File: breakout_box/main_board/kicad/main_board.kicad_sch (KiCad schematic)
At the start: 36 parts, among them CN1 19PIN_LEMO, Q1 DMP3099L, Q2 TIP122

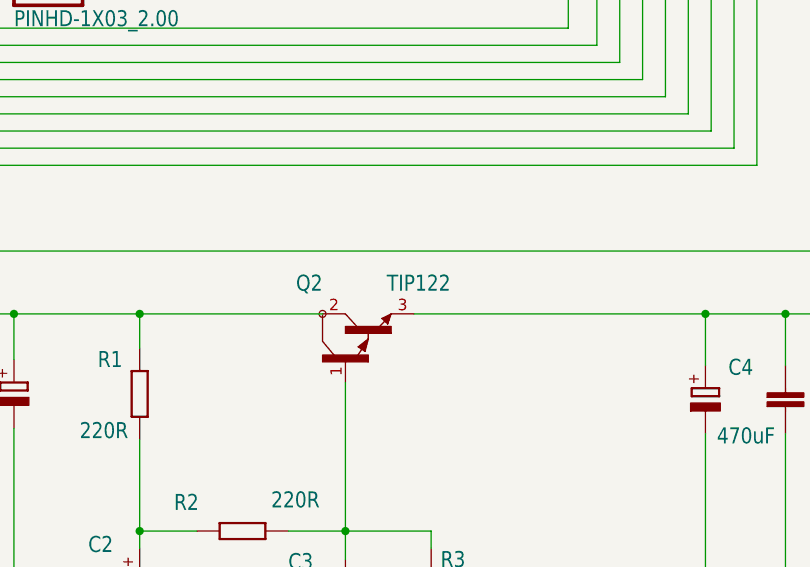
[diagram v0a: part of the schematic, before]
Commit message: Changed transistor to SMD type
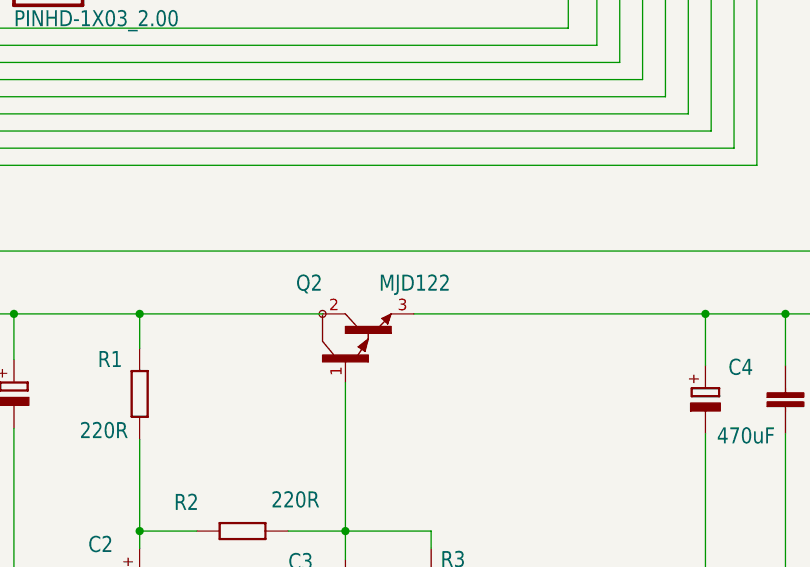
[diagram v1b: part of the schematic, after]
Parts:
- Q2: value TIP122 -> MJD122; footprint main_board:TO-220H -> Package_TO_SOT_SMD:TO-252-2; LCSC (none) -> C59488
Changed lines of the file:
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@@
       (effects (font (size 1.778 1.5113)) (justify left bottom))
     )
-    (property "Value" "TIP122" (id 1) (at 218.059 225.425 90)
+    (property "Value" "MJD122" (id 1) (at 218.059 225.425 90)
       (effects (font (size 1.778 1.5113)) (justify left bottom))
     )
-    (property "Footprint" "main_board:TO-220H" (id 2) (at 206.375 232.41 0)
+    (property "Footprint" "Package_TO_SOT_SMD:TO-252-2" (id 2) (at 206.375 232.41 0)
       (effects (font (size 1.27 1.27)) hide)
     )
     (property "Datasheet" "" (id 3) (at 206.375 232.41 0)
+      (effects (font (size 1.27 1.27)) hide)
+    )
+    (property "LCSC" "C59488" (id 4) (at 206.375 232.41 90)
       (effects (font (size 1.27 1.27)) hide)
     )
@@
     )
     (path "/fba4920e-fdf5-46ca-bff8-f6116ea09a34"
-      (reference "Q2") (unit 1) (value "TIP122") (footprint "main_board:TO-220H")
+      (reference "Q2") (unit 1) (value "MJD122") (footprint "Package_TO_SOT_SMD:TO-252-2")
     )
     (path "/a5d2a7d4-11d3-4ff9-a61d-2d4964edff84"

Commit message: Clean update for KiCad
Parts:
- removed GND1: TH-PAD-1.6/0.8, main_board:TH-PAD-1.6_0.8, symbol main_board-eagle-import:TH-PAD-1.6/0.8
- C5, C6: footprint main_board:C0603 -> Capacitor_SMD:C_0603_1608Metric
- H17, H3, H4, H7, H8: footprint main_board:MA08-1 -> Connector_PinHeader_2.54mm:PinHeader_1x08_P2.54mm_Vertical
- Q1: footprint main_board:SOT23 -> Package_TO_SOT_SMD:SOT-23; JLCPCB_CORRECTION (none) -> 0;0;270
- Q2: JLCPCB_CORRECTION (none) -> 0;0;180
- R1, R2, R3: footprint main_board:R0603 -> Resistor_SMD:R_0603_1608Metric
- R4: footprint main_board:R0402 -> Resistor_SMD:R_0805_2012Metric; LCSC C25900 -> C17673
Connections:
- net CH1: now reaches CN1.P$1 (1), H17.1, H2.1, H3.1

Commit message: Very clean port to KiCAD
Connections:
- net CH2: now reaches CN1.P$2 (2), H17.2, H2.2, H3.2
- net CH3: now reaches CN1.P$3 (3), H17.3, H2.3, H3.3
- net CH4: now reaches CN1.P$4 (4), H17.4, H2.4, H3.4
- net CH5: now reaches CN1.P$5 (5), H17.5, H2.5, H3.5
- net CH6: now reaches CN1.P$6 (6), H17.6, H2.6, H3.6
- net CH7_A: now reaches H2.7, H3.7, JP1.1
- net CH8_A: now reaches H2.8, H3.8, JP2.1
- net CH7_SW: now reaches H1.1, H17.8, JP1.3
- net CH8_SW: now reaches H1.2, H7.1, JP2.3
- net CH9_SW: now reaches H1.3, H7.2, JP3.3
- net CH10_CV: now reaches H1.4, H7.3, JP4.3
- net CH11_CV: now reaches H1.5, H7.4, JP5.3
- net CH12_CV: now reaches H1.6, H7.5, JP6.3
- net CH13_CV: now reaches H1.7, H7.6, JP7.3
- net CH14_CV: now reaches H1.8, H7.7, JP8.3
- net CH15_CV: now reaches H1.9, H7.8, JP9.3
- net CH10: now reaches CN1.P$10 (10), JP4.2
- net CH11: now reaches CN1.P$11 (11), JP5.2
- net CH12: now reaches CN1.P$12 (12), JP13.2
- net CH13: now reaches CN1.P$13 (13), JP12.2
- net CH14: now reaches CN1.P$14 (14), JP11.2
- net CH15: now reaches CN1.P$15 (15), JP10.2
- net CH7: now reaches CN1.P$7 (7), JP1.2
- net CH8: now reaches CN1.P$8 (8), JP2.2
- net CH9: now reaches CN1.P$9 (9), JP3.2
- net CH11_A: now reaches H2.11, H4.3, JP5.1
- net CH10_A: now reaches H2.10, H4.2, JP4.1
- net CH15_A: now reaches H2.15, JP9.1
- net CH9_A: now reaches H17.7, H2.9, H4.1, JP3.1
- net CH13_A: now reaches H2.13, JP7.1
- net CH14_A: now reaches H2.14, JP8.1
- net CH12_A: now reaches H2.12, H4.4, JP6.1
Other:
- note added: "19-Pin LEMO"
- note added: "Config"
- note added: "Expansion"
- note added: "GK-MIDI I/0"
- note added: "Main Board for Nexus Project by Cycfi Research is licensed under a Creative Commons Attribution -ShareAlike 4.0 International License. Copyright CYCFI Research Inc. 2013-2022"
- note added: "Main I/O"
- note added: "Power Section"
- note added: "To I/O Module"
- note removed: "A"
- note removed: "CV/ SW"
- note removed: "Infinity"
- note removed: "Main Board"
- note removed: "Main Board for Nexus Project by Cycfi Research is licensed under a Creative Commons Attribution -ShareAlike 4.0 International License. Copyright CYCFI Research Inc. 2013-2020"
- note removed: "Nexus"
- note removed: "To IO Module"
- company: (none) -> Document Number: 2022011
- title: (none) -> Nexus Main Board
- moved on the sheet: C1, C2, C3, C4, C5, C6, CN1, H1, H17, H2, H3, H4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

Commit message: Main board updates
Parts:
- Q1: JLCPCB_CORRECTION 0;0;270 -> (none); LCSC C155244 -> C2940610
- Q2: JLCPCB_CORRECTION 0;0;180 -> (none)
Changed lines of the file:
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@@
       (effects (font (size 1.27 1.27)) hide)
     )
-    (property "LCSC" "C155244" (id 4) (at 144.78 196.85 0)
+    (property "LCSC" "C2940610" (id 4) (at 144.78 196.85 0)
       (effects (font (size 1.27 1.27)) hide)
     )
-    (property "JLCPCB_CORRECTION" "0;0;270" (id 5) (at 144.78 196.85 90)
+    (property "JLCPCB_CORRECTION" "" (id 5) (at 144.78 196.85 90)
       (effects (font (size 1.27 1.27)) hide)
     )
@@
       (effects (font (size 1.27 1.27)) hide)
     )
-    (property "JLCPCB_CORRECTION" "0;0;180" (id 5) (at 203.2 199.39 90)
+    (property "JLCPCB_CORRECTION" "" (id 5) (at 203.2 199.39 90)
       (effects (font (size 1.27 1.27)) hide)
     )
